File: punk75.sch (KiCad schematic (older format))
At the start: 184 parts, among them J1 AVR-ISP-6, SW1 RESET, SW2 BOOT, U1 ATmega32A-PU, Y1 16MHz

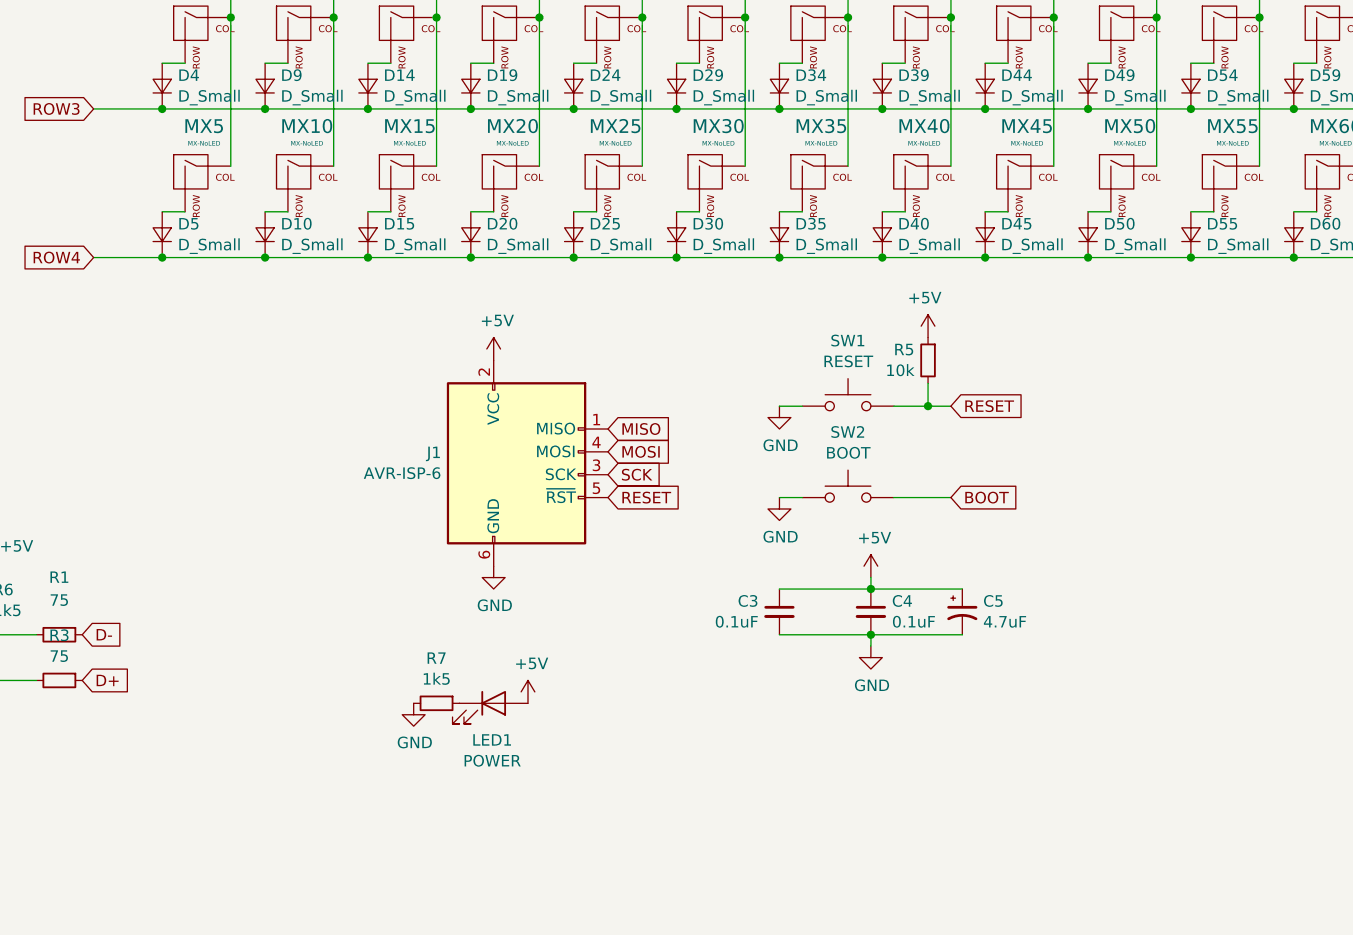
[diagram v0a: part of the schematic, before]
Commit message: added extra switches to allow 2u in bottom row
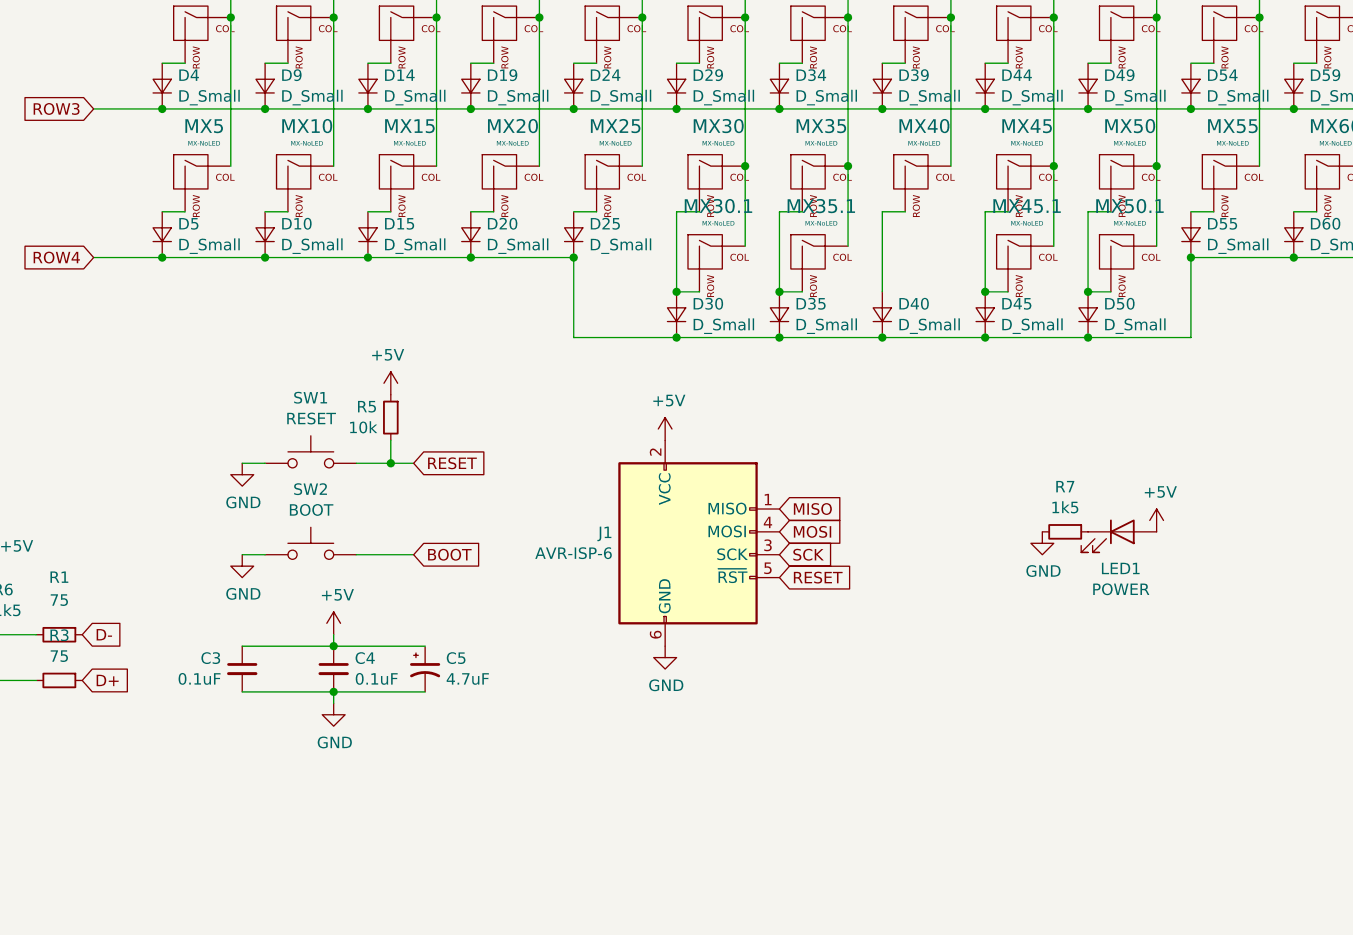
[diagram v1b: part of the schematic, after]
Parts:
- added MX30.1, MX35.1, MX45.1, MX50.1: MX-NoLED, modded_footprints:MXOnly-1U-NoLED, symbol MX_Alps_Hybrid:MX-NoLED
- MX1, MX10, MX11, MX12, MX13, MX14, MX15, MX16, MX17, MX18, MX19, MX2, MX20, MX21, MX22, MX23, MX24, MX25, MX26, MX27, MX28, MX29, MX3, MX30, MX31, MX32, MX33, MX34, MX35, MX36, MX37, MX38, MX39, MX4, MX40, MX41, MX42, MX43, MX44, MX45, MX46, MX47, MX48, MX49, MX5, MX50, MX51, MX52, MX53, MX54, MX55, MX56, MX57, MX58, MX59, MX6, MX60, MX61, MX62, MX63, MX64, MX65, MX66, MX67, MX68, MX69, MX7, MX70, MX71, MX72, MX73, MX74, MX75, MX8, MX9: footprint modded_footprints:MX-1U-NoLED -> modded_footprints:MXOnly-1U-NoLED
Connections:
- net COL5: now also MX30.1.1 (COL)
- net COL6: now also MX35.1.1 (COL)
- net COL8: now also MX45.1.1 (COL)
- net COL9: now also MX50.1.1 (COL)
- net at D30.2 (A), MX30.2 (ROW): now also MX30.1.2 (ROW)
- net at D35.2 (A), MX35.2 (ROW): now also MX35.1.2 (ROW)
- net at D45.2 (A), MX45.2 (ROW): now also MX45.1.2 (ROW)
- net at D50.2 (A), MX50.2 (ROW): now also MX50.1.2 (ROW)
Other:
- moved on the sheet: C3, C4, C5, D30, D35, D40, D45, D50, J1, LED1, R5, R7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

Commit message: changed footprints to my modded MX-Alps hybrids
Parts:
- MX1, MX10, MX11, MX12, MX13, MX14, MX15, MX16, MX17, MX18, MX19, MX2, MX20, MX21, MX22, MX23, MX24, MX25, MX26, MX27, MX28, MX29, MX3, MX30, MX31, MX32, MX33, MX34, MX35, MX36, MX37, MX38, MX39, MX4, MX40, MX41, MX42, MX43, MX44, MX45, MX46, MX47, MX48, MX49, MX5, MX50, MX51, MX52, MX53, MX54, MX55, MX56, MX57, MX58, MX59, MX6, MX60, MX61, MX62, MX63, MX64, MX65, MX66, MX67, MX68, MX69, MX7, MX70, MX71, MX72, MX73, MX74, MX75, MX8, MX9: footprint modded_footprints:MXOnly-1U-NoLED -> MX_Alps_Hybrid:MX-1U-NoLED
- MX30.1, MX35.1, MX45.1, MX50.1: footprint modded_footprints:MXOnly-1U-NoLED -> MX_Alps_Hybrid:MX-2U-NoLED

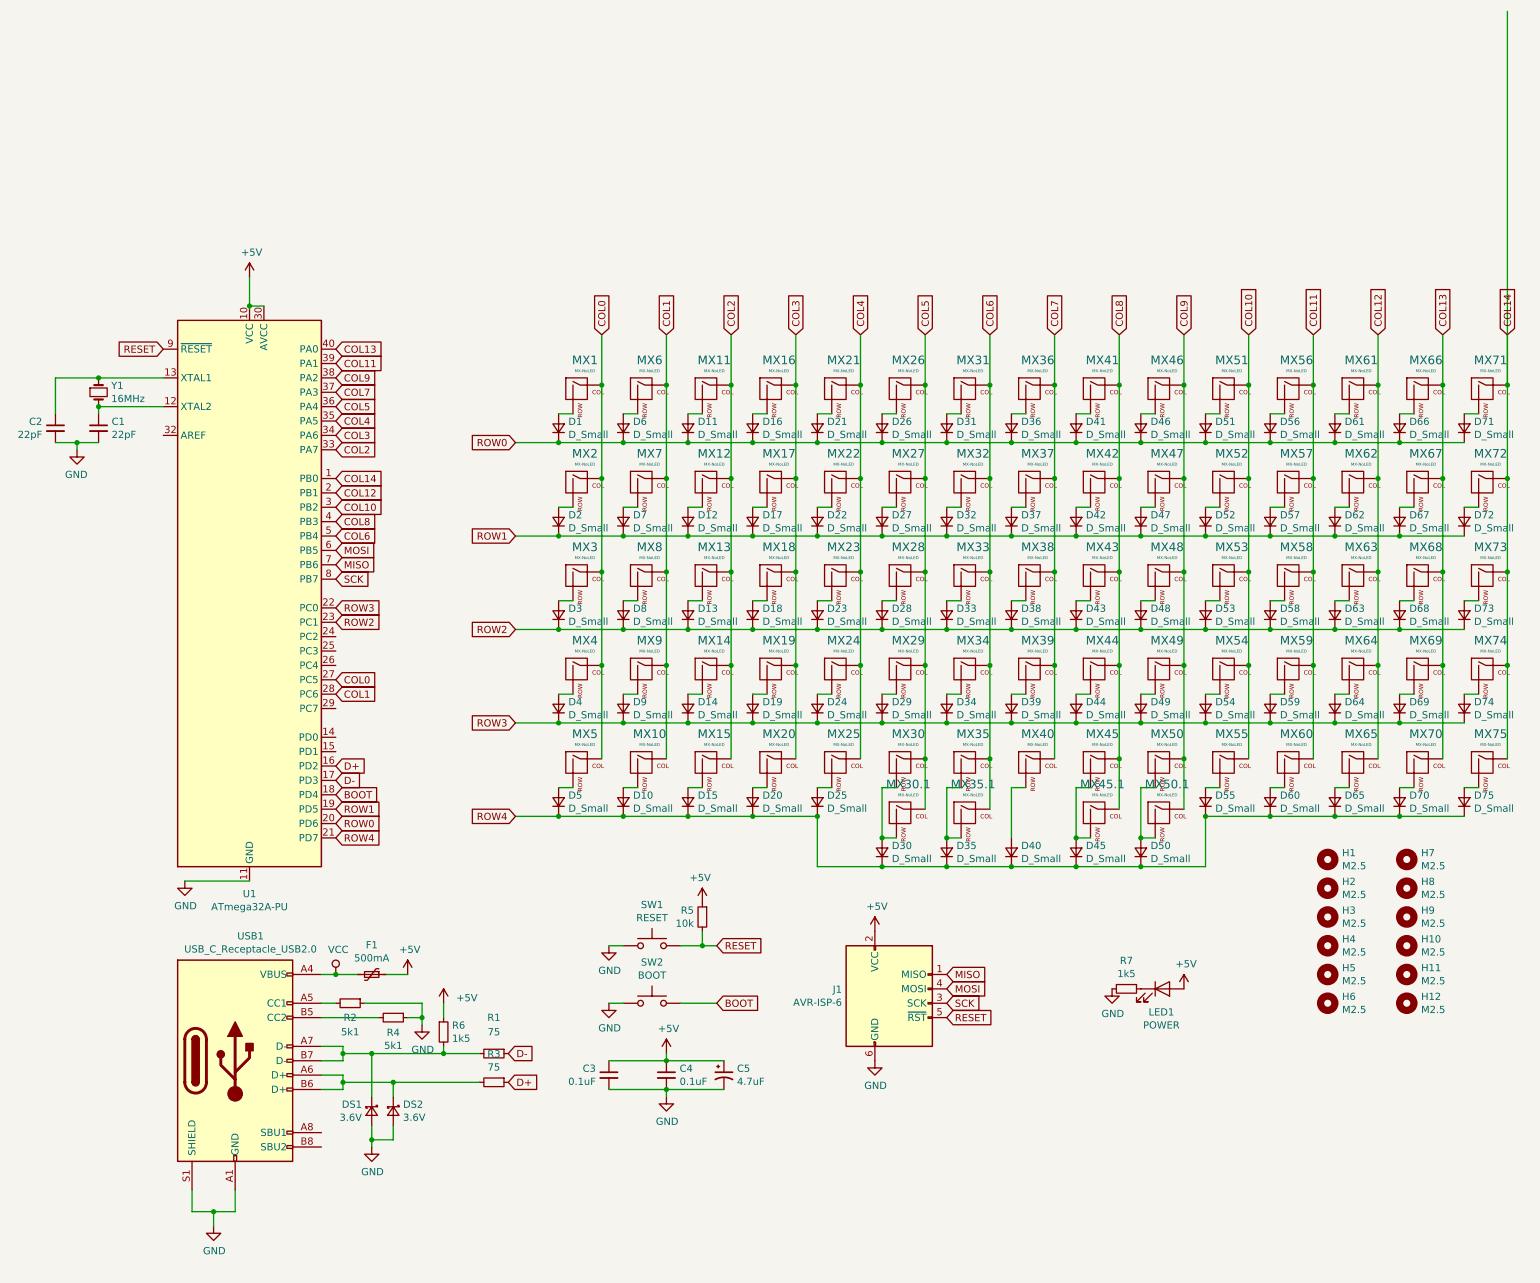
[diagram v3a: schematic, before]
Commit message: added configurable led and rewired all colums to new ports
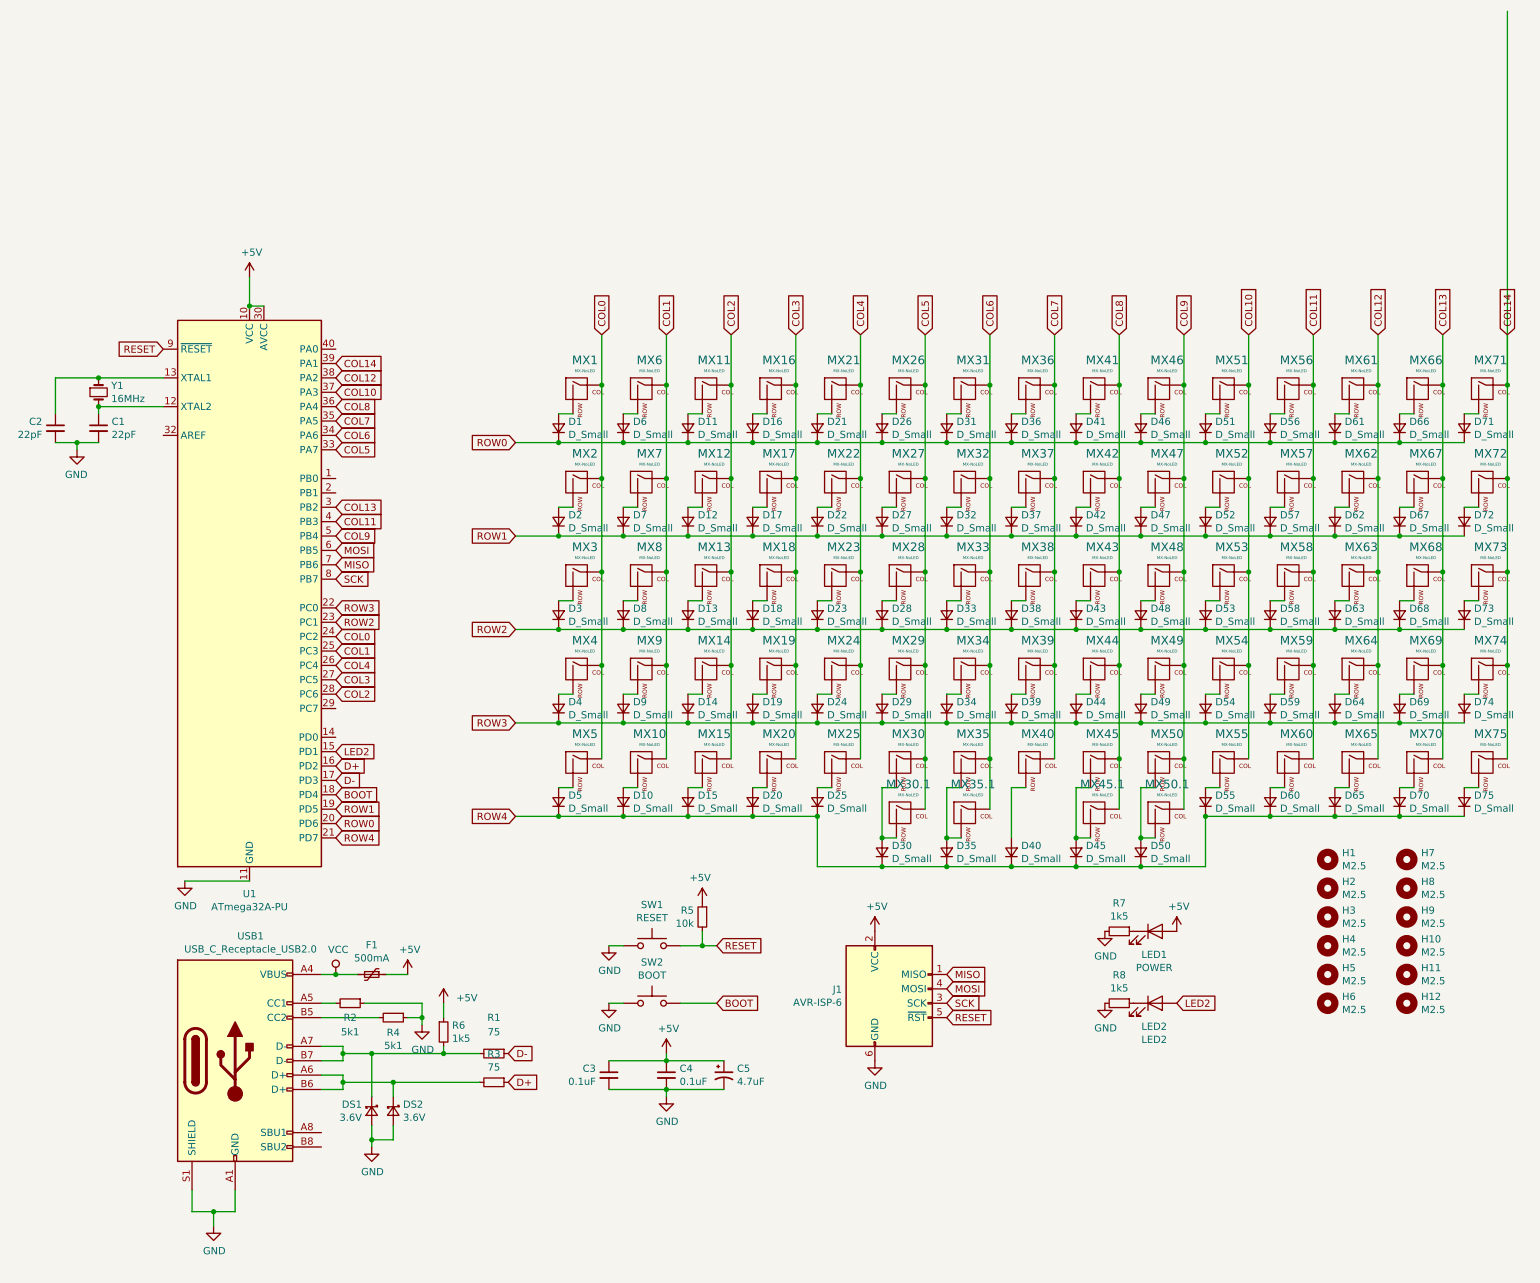
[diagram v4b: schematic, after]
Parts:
- added LED2: LED2, LED_THT:LED_D3.0mm, symbol Device:LED
- added R8: 1k5, Resistor_THT:R_Axial_DIN0204_L3.6mm_D1.6mm_P5.08mm_Horizontal, symbol Device:R_Small
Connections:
- net COL0: now also U1.24 (PC2); no longer U1.27 (PC5)
- net COL1: now also U1.25 (PC3); no longer U1.28 (PC6)
- net COL10: now also U1.37 (PA3); no longer U1.3 (PB2)
- net COL11: now also U1.4 (PB3); no longer U1.39 (PA1)
- net COL12: now also U1.38 (PA2); no longer U1.2 (PB1)
- net COL13: now also U1.3 (PB2); no longer U1.40 (PA0)
- net COL14: now also U1.39 (PA1); no longer U1.1 (PB0)
- net COL2: now also U1.28 (PC6); no longer U1.33 (PA7)
- net COL3: now also U1.27 (PC5); no longer U1.34 (PA6)
- net COL4: now also U1.26 (PC4); no longer U1.35 (PA5)
- net COL5: now also U1.33 (PA7); no longer U1.36 (PA4)
- net COL6: now also U1.34 (PA6); no longer U1.5 (PB4)
- net COL7: now also U1.35 (PA5); no longer U1.37 (PA3)
- net COL8: now also U1.36 (PA4); no longer U1.4 (PB3)
- net COL9: now also U1.5 (PB4); no longer U1.38 (PA2)
- net GND: now also R8.2
- net LED2: now reaches U1.15 (PD1)
- net LED2: now also LED2.2 (A)
- new net: LED2.1 (K), R8.1
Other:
- moved on the sheet: LED1, R7
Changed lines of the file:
@@
 L Device:LED LED1
 U 1 1 5F13B82B
-P 8550 5800
-F 0 "LED1" H 8543 5638 50  0000 C CNN
-F 1 "POWER" H 8543 5547 50  0000 C CNN
-F 2 "LED_THT:LED_D3.0mm" H 8550 5800 50  0001 C CNN
-F 3 "~" H 8550 5800 50  0001 C CNN
-	1    8550 5800
+P 8500 5400
+F 0 "LED1" H 8493 5238 50  0000 C CNN
+F 1 "POWER" H 8493 5147 50  0000 C CNN
+F 2 "LED_THT:LED_D3.0mm" H 8500 5400 50  0001 C CNN
+F 3 "~" H 8500 5400 50  0001 C CNN
+	1    8500 5400
 	1    0    0    -1
 $EndComp
@@
 L Device:R_Small R7
 U 1 1 5F13CDFC
-P 8300 5800
-F 0 "R7" V 8104 5800 50  0000 C CNN
-F 1 "1k5" V 8195 5800 50  0000 C CNN
-F 2 "Resistor_THT:R_Axial_DIN0204_L3.6mm_D1.6mm_P5.08mm_Horizontal" H 8300 5800 50  0001 C CNN
-F 3 "~" H 8300 5800 50  0001 C CNN
-	1    8300 5800
+P 8250 5400
+F 0 "R7" V 8054 5400 50  0000 C CNN
+F 1 "1k5" V 8145 5400 50  0000 C CNN
+F 2 "Resistor_THT:R_Axial_DIN0204_L3.6mm_D1.6mm_P5.08mm_Horizontal" H 8250 5400 50  0001 C CNN
+F 3 "~" H 8250 5400 50  0001 C CNN
+	1    8250 5400
 	0    1    1    0
 $EndComp
@@
 L power:+5V #PWR0117
 U 1 1 5F13EA77
-P 8700 5800
-F 0 "#PWR0117" H 8700 5650 50  0001 C CNN
-F 1 "+5V" H 8715 5973 50  0000 C CNN
-F 2 "" H 8700 5800 50  0001 C CNN
-F 3 "" H 8700 5800 50  0001 C CNN
-	1    8700 5800
+P 8650 5400
+F 0 "#PWR0117" H 8650 5250 50  0001 C CNN
+F 1 "+5V" H 8665 5573 50  0000 C CNN
+F 2 "" H 8650 5400 50  0001 C CNN
+F 3 "" H 8650 5400 50  0001 C CNN
+	1    8650 5400
 	1    0    0    -1
 $EndComp
@@
 L power:GND #PWR0118
 U 1 1 5F13FCEC
-P 8200 5800
-F 0 "#PWR0118" H 8200 5550 50  0001 C CNN
-F 1 "GND" H 8205 5627 50  0000 C CNN
-F 2 "" H 8200 5800 50  0001 C CNN
-F 3 "" H 8200 5800 50  0001 C CNN
-	1    8200 5800
+P 8150 5400
+F 0 "#PWR0118" H 8150 5150 50  0001 C CNN
+F 1 "GND" H 8155 5227 50  0000 C CNN
+F 2 "" H 8150 5400 50  0001 C CNN
+F 3 "" H 8150 5400 50  0001 C CNN
+	1    8150 5400
 	1    0    0    -1
 $EndComp
@@
 Text GLabel 2800 4650 2    50   Input ~ 0
 ROW0
+Text GLabel 2800 3350 2    50   Input ~ 0
+COL0
+Text GLabel 2800 3450 2    50   Input ~ 0
+COL1
+Text GLabel 2800 3750 2    50   Input ~ 0
+COL2
 Text GLabel 2800 3650 2    50   Input ~ 0
-COL0
-Text GLabel 2800 3750 2    50   Input ~ 0
-COL1
+COL3
+Text GLabel 2800 3550 2    50   Input ~ 0
+COL4
+Text GLabel 2800 2450 2    50   Input ~ 0
+COL13
+Text GLabel 2800 2550 2    50   Input ~ 0
+COL11
+Text GLabel 2800 2650 2    50   Input ~ 0
+COL9
+Text GLabel 2800 1850 2    50   Input ~ 0
+COL7
 Text GLabel 2800 2050 2    50   Input ~ 0
-COL2
+COL5
+Text GLabel 2800 1450 2    50   Input ~ 0
+COL14
+Text GLabel 2800 1550 2    50   Input ~ 0
+COL12
+Text GLabel 2800 1650 2    50   Input ~ 0
+COL10
+Text GLabel 2800 1750 2    50   Input ~ 0
+COL8
 Text GLabel 2800 1950 2    50   Input ~ 0
-COL3
-Text GLabel 2800 1850 2    50   Input ~ 0
-COL4
-Text GLabel 2800 1350 2    50   Input ~ 0
-COL13
-Text GLabel 2800 1450 2    50   Input ~ 0
-COL11
-Text GLabel 2800 1550 2    50   Input ~ 0
-COL9
-Text GLabel 2800 1650 2    50   Input ~ 0
-COL7
-Text GLabel 2800 1750 2    50   Input ~ 0
-COL5
-Text GLabel 2800 2250 2    50   Input ~ 0
-COL14
-Text GLabel 2800 2350 2    50   Input ~ 0
-COL12
-Text GLabel 2800 2450 2    50   Input ~ 0
-COL10
-Text GLabel 2800 2550 2    50   Input ~ 0
-COL8
-Text GLabel 2800 2650 2    50   Input ~ 0
 COL6
 $Comp
@@
 	1    0    0    -1
 $EndComp
+$Comp
+L Device:LED LED2
+U 1 1 5ED11032
+P 8500 5900
+F 0 "LED2" H 8493 5738 50  0000 C CNN
+F 1 "LED2" H 8493 5647 50  0000 C CNN
+F 2 "LED_THT:LED_D3.0mm" H 8500 5900 50  0001 C CNN
+F 3 "~" H 8500 5900 50  0001 C CNN
+	1    8500 5900
+	1    0    0    -1
+$EndComp
+$Comp
+L Device:R_Small R8
+U 1 1 5ED1103C
+P 8250 5900
+F 0 "R8" V 8054 5900 50  0000 C CNN
+F 1 "1k5" V 8145 5900 50  0000 C CNN
+F 2 "Resistor_THT:R_Axial_DIN0204_L3.6mm_D1.6mm_P5.08mm_Horizontal" H 8250 5900 50  0001 C CNN
+F 3 "~" H 8250 5900 50  0001 C CNN
+	1    8250 5900
+	0    1    1    0
+$EndComp
+$Comp
+L power:GND #PWR0119
+U 1 1 5ED11046
+P 8150 5900
+F 0 "#PWR0119" H 8150 5650 50  0001 C CNN
+F 1 "GND" H 8155 5727 50  0000 C CNN
+F 2 "" H 8150 5900 50  0001 C CNN
+F 3 "" H 8150 5900 50  0001 C CNN
+	1    8150 5900
+	1    0    0    -1
+$EndComp
+Text GLabel 8650 5900 2    50   Input ~ 0
+LED2
+Text GLabel 2800 4150 2    50   Input ~ 0
+LED2
 $EndSCHEMATC
